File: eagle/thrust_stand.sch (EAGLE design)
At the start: 28 parts, among them IC1 7805TV, Q1 16Mhz, Q2 IRF510, SW1 EC12E_SW, T1 2N3904, U2 ATMEGA328P_PDIP

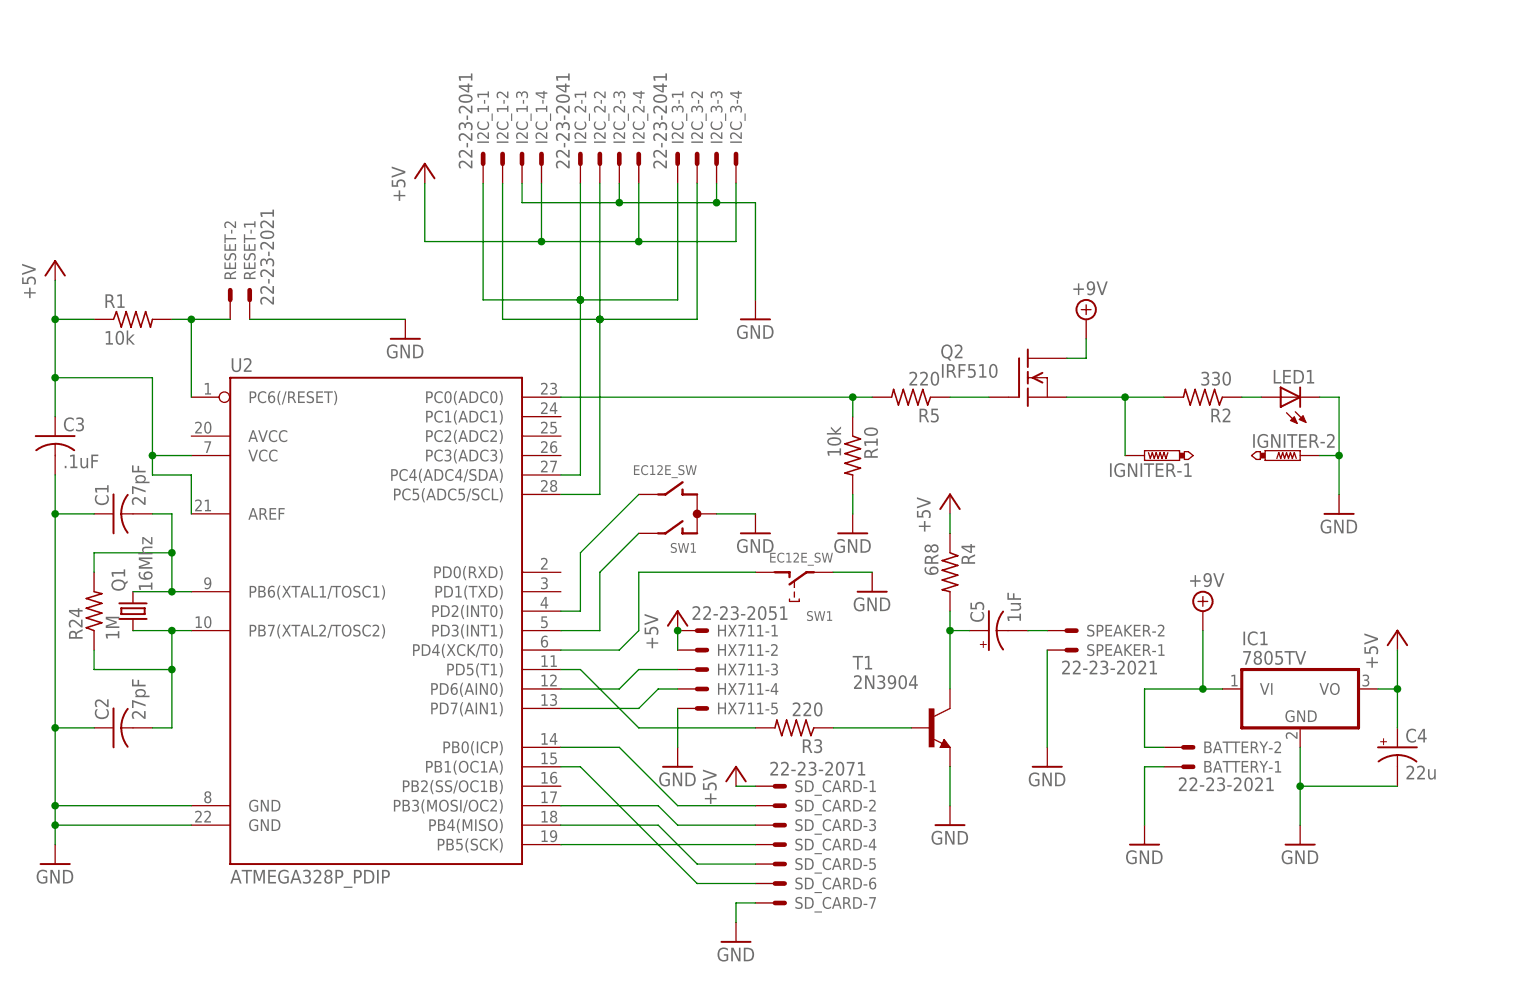
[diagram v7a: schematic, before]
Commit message: igniter moved to supply side and saving calibration value when finished calib
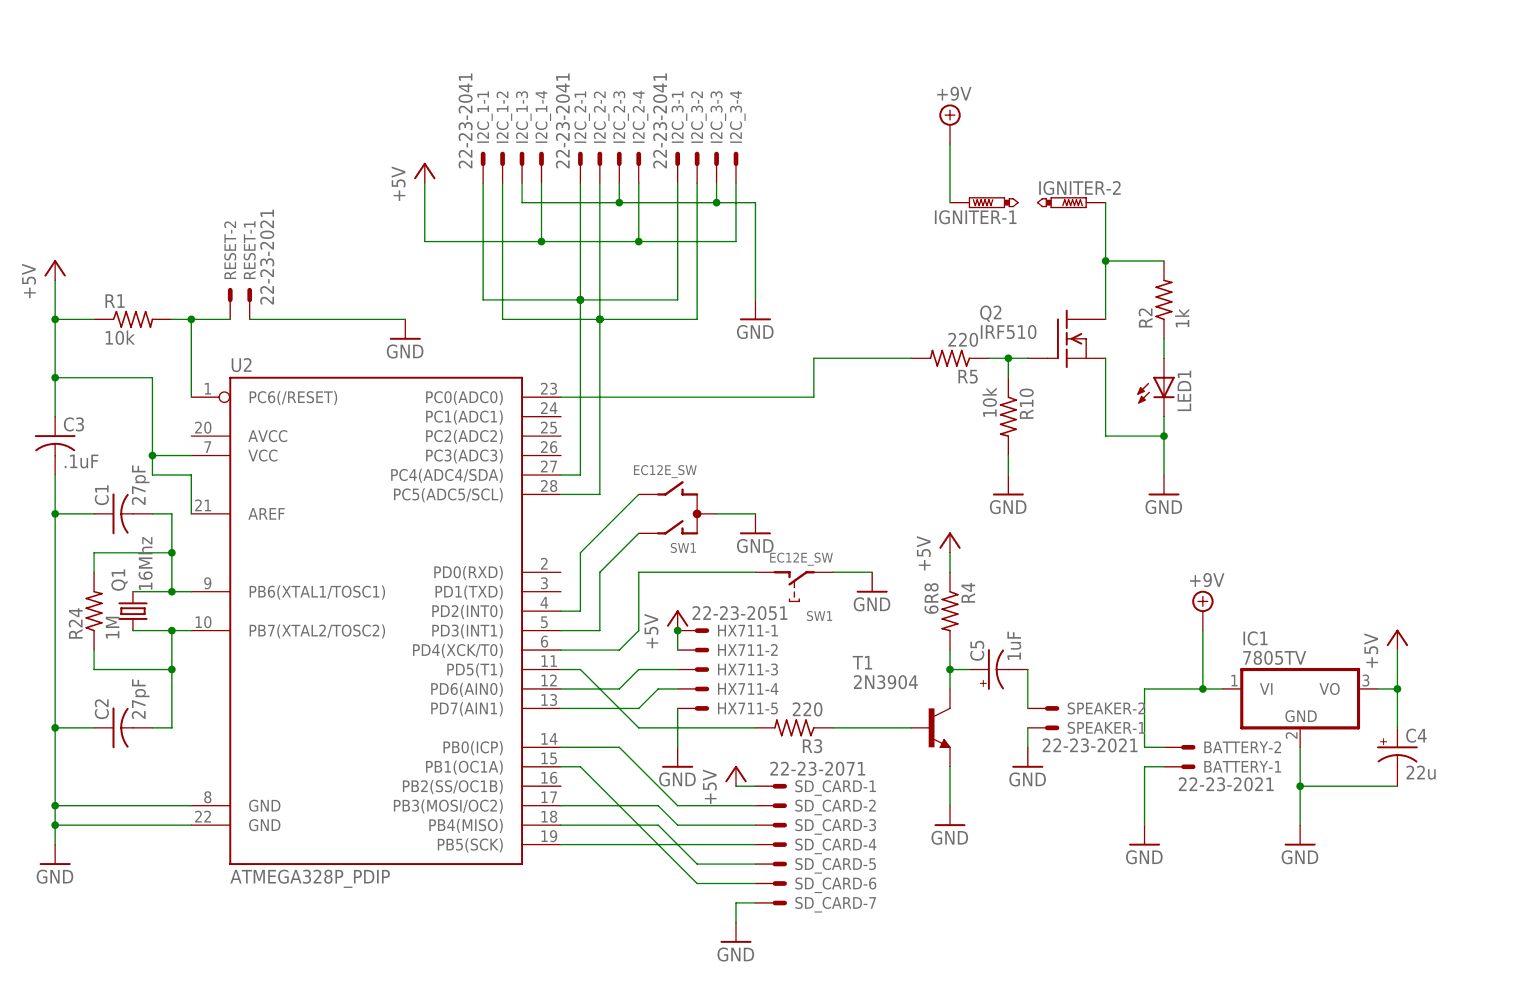
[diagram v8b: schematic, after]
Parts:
- R2: value 330 -> 1k
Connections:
- removed net N$24: IGNITER-1.TP, Q2.S, R2.2
- new net N$17: IGNITER-2.TP, Q2.D, R2.2
- net +9V: now also IGNITER-1.TP; no longer Q2.D
- net GND: now also Q2.S; no longer IGNITER-2.TP
- net N$12: now also R10.1
- net N$18: no longer R10.1
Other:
- moved on the sheet: C5, IGNITER-1, IGNITER-2, LED1, Q2, R10, R2, R4, R5, SPEAKER-1, SPEAKER-2
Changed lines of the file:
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@@
 <?xml version="1.0" encoding="utf-8"?>
 <!DOCTYPE eagle SYSTEM "eagle.dtd">
-<eagle version="7.7.0">
+<eagle version="7.6.0">
 <drawing>
 <settings>
@@
 <part name="Q2" library="transistor-fet" deviceset="IRF510" device=""/>
 <part name="SUPPLY1" library="supply2" deviceset="+9V" device=""/>
-<part name="R2" library="rcl" deviceset="R-US_" device="0207/7" value="330"/>
+<part name="R2" library="rcl" deviceset="R-US_" device="0207/7" value="1k"/>
 <part name="LED1" library="led" deviceset="LED" device="5MM"/>
 <part name="GND6" library="supply1" deviceset="GND" device=""/>
@@
 <instance part="P+3" gate="1" x="22.86" y="104.14"/>
 <instance part="GND3" gate="1" x="66.04" y="83.82"/>
-<instance part="Q2" gate="G$1" x="101.6" y="76.2"/>
-<instance part="SUPPLY1" gate="G$1" x="109.22" y="83.82"/>
-<instance part="R2" gate="G$1" x="124.46" y="73.66" rot="R180"/>
-<instance part="LED1" gate="G$1" x="134.62" y="73.66" rot="R90"/>
-<instance part="GND6" gate="1" x="142.24" y="58.42"/>
+<instance part="Q2" gate="G$1" x="106.68" y="81.28"/>
+<instance part="SUPPLY1" gate="G$1" x="91.44" y="109.22"/>
+<instance part="R2" gate="G$1" x="119.38" y="86.36" rot="R90"/>
+<instance part="LED1" gate="G$1" x="119.38" y="76.2"/>
+<instance part="GND6" gate="1" x="119.38" y="60.96"/>
 <instance part="IC1" gate="A1" x="137.16" y="35.56"/>
 <instance part="SUPPLY2" gate="G$1" x="124.46" y="45.72"/>
@@
 <instance part="BATTERY" gate="-2" x="121.92" y="27.94" rot="MR180"/>
 <instance part="GND9" gate="1" x="116.84" y="15.24"/>
-<instance part="R5" gate="G$1" x="86.36" y="73.66" rot="R180"/>
-<instance part="R10" gate="G$1" x="78.74" y="66.04" rot="R270"/>
-<instance part="GND5" gate="1" x="78.74" y="55.88"/>
+<instance part="R5" gate="G$1" x="91.44" y="78.74" rot="R180"/>
+<instance part="R10" gate="G$1" x="99.06" y="71.12" rot="R270"/>
+<instance part="GND5" gate="1" x="99.06" y="60.96"/>
 <instance part="HX711" gate="-1" x="58.42" y="43.18"/>
 <instance part="HX711" gate="-2" x="58.42" y="40.64"/>
@@
 <instance part="T1" gate="G1" x="88.9" y="30.48"/>
 <instance part="R3" gate="G$1" x="71.12" y="30.48" rot="R180"/>
-<instance part="C5" gate="G$1" x="96.52" y="43.18" rot="R90"/>
-<instance part="SPEAKER" gate="-1" x="106.68" y="40.64" rot="MR180"/>
-<instance part="SPEAKER" gate="-2" x="106.68" y="43.18" rot="MR180"/>
-<instance part="R4" gate="G$1" x="91.44" y="50.8" rot="R270"/>
-<instance part="P+5" gate="1" x="91.44" y="60.96"/>
+<instance part="C5" gate="G$1" x="96.52" y="38.1" rot="R90"/>
+<instance part="SPEAKER" gate="-1" x="104.14" y="30.48" rot="MR180"/>
+<instance part="SPEAKER" gate="-2" x="104.14" y="33.02" rot="MR180"/>
+<instance part="R4" gate="G$1" x="91.44" y="45.72" rot="R270"/>
+<instance part="P+5" gate="1" x="91.44" y="55.88"/>
 <instance part="GND7" gate="1" x="91.44" y="17.78"/>
-<instance part="GND10" gate="1" x="104.14" y="25.4"/>
-<instance part="IGNITER" gate="-1" x="116.84" y="66.04" rot="R90"/>
-<instance part="IGNITER" gate="-2" x="137.16" y="66.04" rot="R270"/>
+<instance part="GND10" gate="1" x="101.6" y="25.4"/>
+<instance part="IGNITER" gate="-1" x="93.98" y="99.06" rot="R90"/>
+<instance part="IGNITER" gate="-2" x="109.22" y="99.06" rot="R270"/>
 <instance part="SW1" gate="G$1" x="58.42" y="58.42" rot="R90"/>
 <instance part="SW1" gate="G$2" x="71.12" y="50.8" rot="R180"/>
@@
 <pinref part="R4" gate="G$1" pin="1"/>
 <pinref part="P+5" gate="1" pin="+5V"/>
-<wire x1="91.44" y1="55.88" x2="91.44" y2="58.42" width="0.1524" layer="91"/>
+<wire x1="91.44" y1="50.8" x2="91.44" y2="53.34" width="0.1524" layer="91"/>
 </segment>
 </net>
@@
 <pinref part="GND5" gate="1" pin="GND"/>
 <pinref part="R10" gate="G$1" pin="2"/>
-<wire x1="78.74" y1="60.96" x2="78.74" y2="58.42" width="0.1524" layer="91"/>
+<wire x1="99.06" y1="66.04" x2="99.06" y2="63.5" width="0.1524" layer="91"/>
 </segment>
 <segment>
 <pinref part="LED1" gate="G$1" pin="C"/>
-<wire x1="139.7" y1="73.66" x2="142.24" y2="73.66" width="0.1524" layer="91"/>
-<wire x1="142.24" y1="73.66" x2="142.24" y2="66.04" width="0.1524" layer="91"/>
-<wire x1="139.7" y1="66.04" x2="142.24" y2="66.04" width="0.1524" layer="91"/>
+<wire x1="119.38" y1="71.12" x2="119.38" y2="68.58" width="0.1524" layer="91"/>
 <pinref part="GND6" gate="1" pin="GND"/>
-<wire x1="142.24" y1="66.04" x2="142.24" y2="60.96" width="0.1524" layer="91"/>
-<junction x="142.24" y="66.04"/>
-<pinref part="IGNITER" gate="-2" pin="TP"/>
+<pinref part="Q2" gate="G$1" pin="S"/>
+<wire x1="119.38" y1="68.58" x2="119.38" y2="63.5" width="0.1524" layer="91"/>
+<wire x1="111.76" y1="78.74" x2="111.76" y2="68.58" width="0.1524" layer="91"/>
+<wire x1="111.76" y1="68.58" x2="119.38" y2="68.58" width="0.1524" layer="91"/>
+<junction x="119.38" y="68.58"/>
 </segment>
 <segment>
@@
 <pinref part="SPEAKER" gate="-1" pin="S"/>
 <pinref part="GND10" gate="1" pin="GND"/>
-<wire x1="104.14" y1="40.64" x2="104.14" y2="27.94" width="0.1524" layer="91"/>
+<wire x1="101.6" y1="30.48" x2="101.6" y2="27.94" width="0.1524" layer="91"/>
 </segment>
 <segment>
@@
 <net name="+9V" class="0">
 <segment>
-<pinref part="SUPPLY1" gate="G$1" pin="+9V"/>
-<wire x1="109.22" y1="78.74" x2="109.22" y2="81.28" width="0.1524" layer="91"/>
-<pinref part="Q2" gate="G$1" pin="D"/>
-<wire x1="106.68" y1="78.74" x2="109.22" y2="78.74" width="0.1524" layer="91"/>
-</segment>
-<segment>
 <pinref part="IC1" gate="A1" pin="VI"/>
 <wire x1="127" y1="35.56" x2="124.46" y2="35.56" width="0.1524" layer="91"/>
@@
 <junction x="124.46" y="35.56"/>
 </segment>
+<segment>
+<pinref part="IGNITER" gate="-1" pin="TP"/>
+<pinref part="SUPPLY1" gate="G$1" pin="+9V"/>
+<wire x1="91.44" y1="99.06" x2="91.44" y2="106.68" width="0.1524" layer="91"/>
+</segment>
 </net>
 <net name="N$18" class="0">
 <segment>
 <pinref part="U2" gate="G$1" pin="PC0(ADC0)"/>
-<wire x1="40.64" y1="73.66" x2="78.74" y2="73.66" width="0.1524" layer="91"/>
-<wire x1="78.74" y1="73.66" x2="81.28" y2="73.66" width="0.1524" layer="91"/>
+<wire x1="40.64" y1="73.66" x2="73.66" y2="73.66" width="0.1524" layer="91"/>
+<wire x1="73.66" y1="73.66" x2="73.66" y2="78.74" width="0.1524" layer="91"/>
+<wire x1="73.66" y1="78.74" x2="86.36" y2="78.74" width="0.1524" layer="91"/>
 <pinref part="R5" gate="G$1" pin="2"/>
-<pinref part="R10" gate="G$1" pin="1"/>
-<wire x1="78.74" y1="71.12" x2="78.74" y2="73.66" width="0.1524" layer="91"/>
-<junction x="78.74" y="73.66"/>
 </segment>
 </net>
@@
 <pinref part="R2" gate="G$1" pin="1"/>
 <pinref part="LED1" gate="G$1" pin="A"/>
-<wire x1="132.08" y1="73.66" x2="129.54" y2="73.66" width="0.1524" layer="91"/>
-</segment>
-</net>
-<net name="N$24" class="0">
-<segment>
-<pinref part="Q2" gate="G$1" pin="S"/>
-<pinref part="R2" gate="G$1" pin="2"/>
-<wire x1="106.68" y1="73.66" x2="114.3" y2="73.66" width="0.1524" layer="91"/>
-<wire x1="114.3" y1="73.66" x2="119.38" y2="73.66" width="0.1524" layer="91"/>
-<wire x1="114.3" y1="66.04" x2="114.3" y2="73.66" width="0.1524" layer="91"/>
-<junction x="114.3" y="73.66"/>
-<pinref part="IGNITER" gate="-1" pin="TP"/>
+<wire x1="119.38" y1="78.74" x2="119.38" y2="81.28" width="0.1524" layer="91"/>
 </segment>
 </net>
@@
 <pinref part="Q2" gate="G$1" pin="G"/>
 <pinref part="R5" gate="G$1" pin="1"/>
-<wire x1="91.44" y1="73.66" x2="96.52" y2="73.66" width="0.1524" layer="91"/>
+<wire x1="96.52" y1="78.74" x2="99.06" y2="78.74" width="0.1524" layer="91"/>
+<pinref part="R10" gate="G$1" pin="1"/>
+<wire x1="99.06" y1="78.74" x2="101.6" y2="78.74" width="0.1524" layer="91"/>
+<wire x1="99.06" y1="76.2" x2="99.06" y2="78.74" width="0.1524" layer="91"/>
+<junction x="99.06" y="78.74"/>
 </segment>
 </net>
@@
 <pinref part="T1" gate="G1" pin="C"/>
 <pinref part="R4" gate="G$1" pin="2"/>
-<wire x1="91.44" y1="35.56" x2="91.44" y2="43.18" width="0.1524" layer="91"/>
+<wire x1="91.44" y1="35.56" x2="91.44" y2="38.1" width="0.1524" layer="91"/>
 <pinref part="C5" gate="G$1" pin="+"/>
-<wire x1="91.44" y1="43.18" x2="91.44" y2="45.72" width="0.1524" layer="91"/>
-<wire x1="93.98" y1="43.18" x2="91.44" y2="43.18" width="0.1524" layer="91"/>
-<junction x="91.44" y="43.18"/>
+<wire x1="91.44" y1="38.1" x2="91.44" y2="40.64" width="0.1524" layer="91"/>
+<wire x1="93.98" y1="38.1" x2="91.44" y2="38.1" width="0.1524" layer="91"/>
+<junction x="91.44" y="38.1"/>
 </segment>
 </net>
@@
 <pinref part="SPEAKER" gate="-2" pin="S"/>
 <pinref part="C5" gate="G$1" pin="-"/>
-<wire x1="104.14" y1="43.18" x2="101.6" y2="43.18" width="0.1524" layer="91"/>
+<wire x1="101.6" y1="33.02" x2="101.6" y2="38.1" width="0.1524" layer="91"/>
 </segment>
 </net>
@@
 </segment>
 </net>
+<net name="N$17" class="0">
+<segment>
+<pinref part="Q2" gate="G$1" pin="D"/>
+<pinref part="IGNITER" gate="-2" pin="TP"/>
+<wire x1="111.76" y1="83.82" x2="111.76" y2="91.44" width="0.1524" layer="91"/>
+<pinref part="R2" gate="G$1" pin="2"/>
+<wire x1="111.76" y1="91.44" x2="111.76" y2="99.06" width="0.1524" layer="91"/>
+<wire x1="119.38" y1="91.44" x2="111.76" y2="91.44" width="0.1524" layer="91"/>
+<junction x="111.76" y="91.44"/>
+</segment>
+</net>
